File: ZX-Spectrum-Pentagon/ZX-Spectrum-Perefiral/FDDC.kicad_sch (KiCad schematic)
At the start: 39 parts

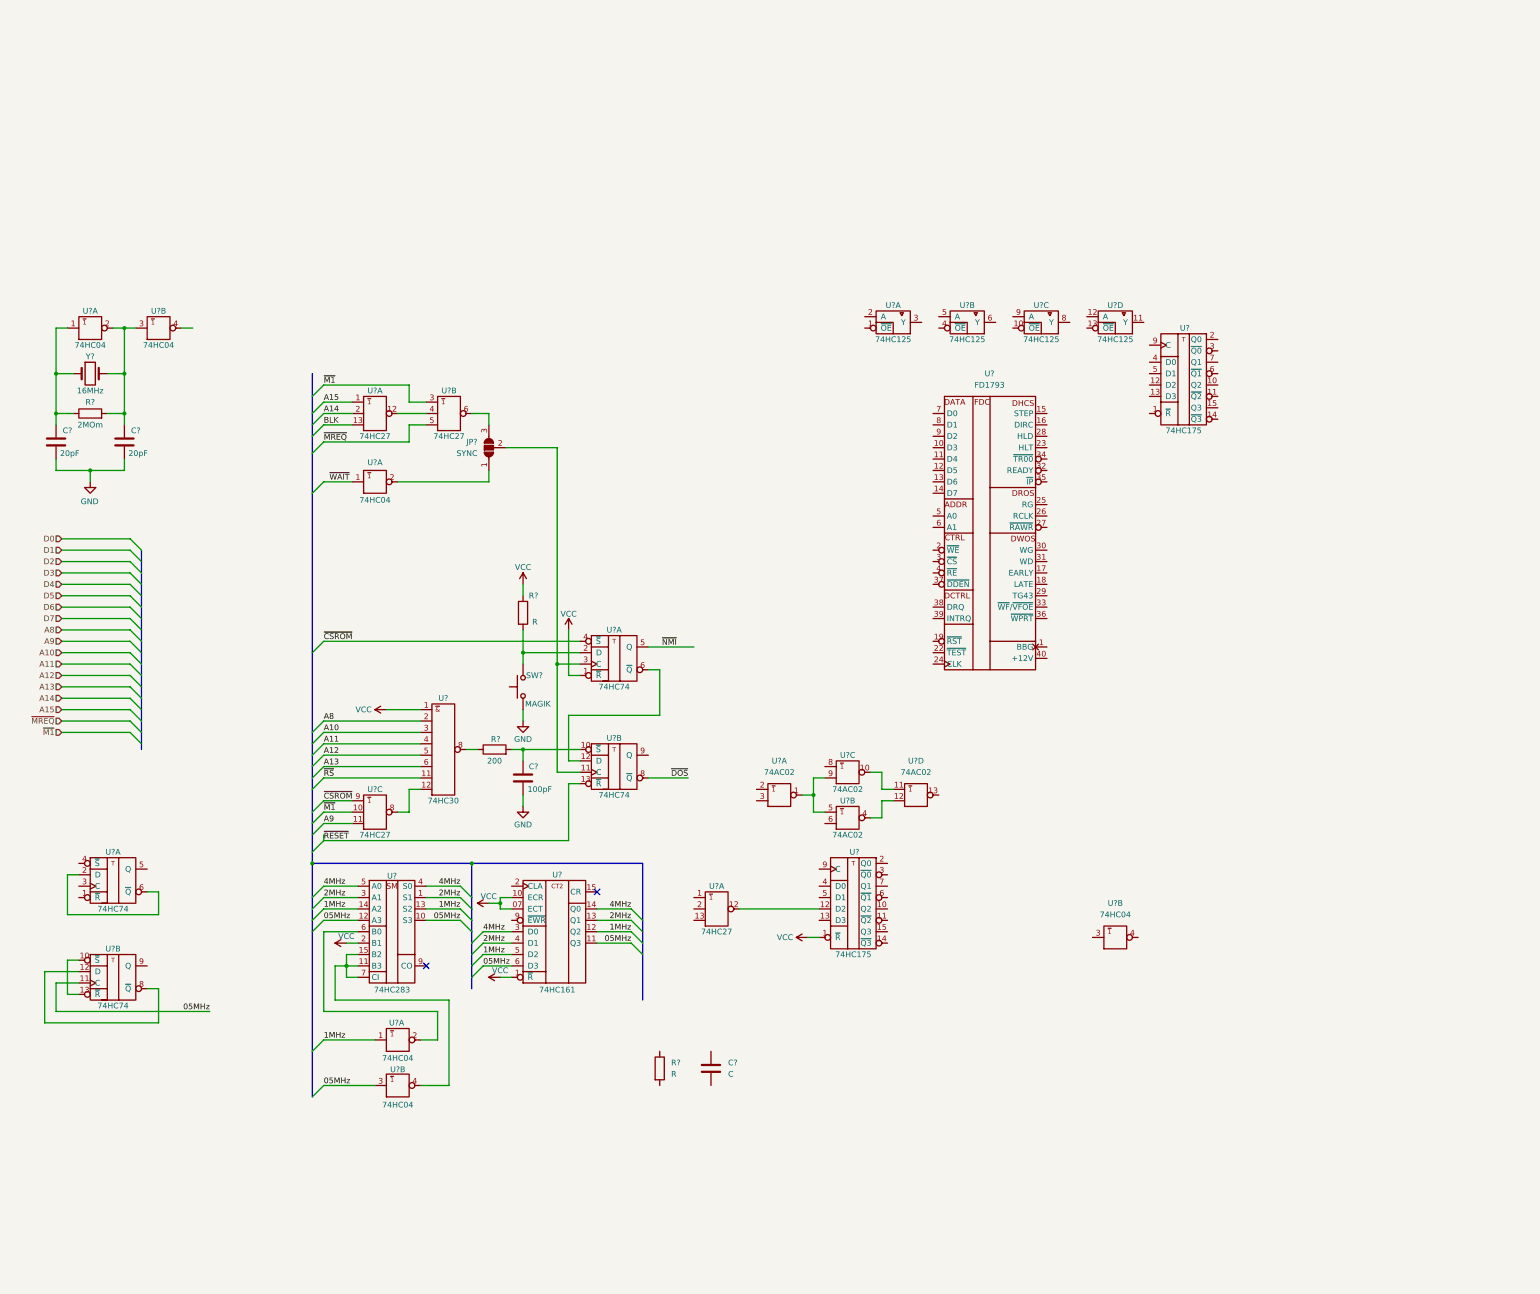
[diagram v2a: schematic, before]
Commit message: CPU.kicad_sch non functional changes update fdd controller
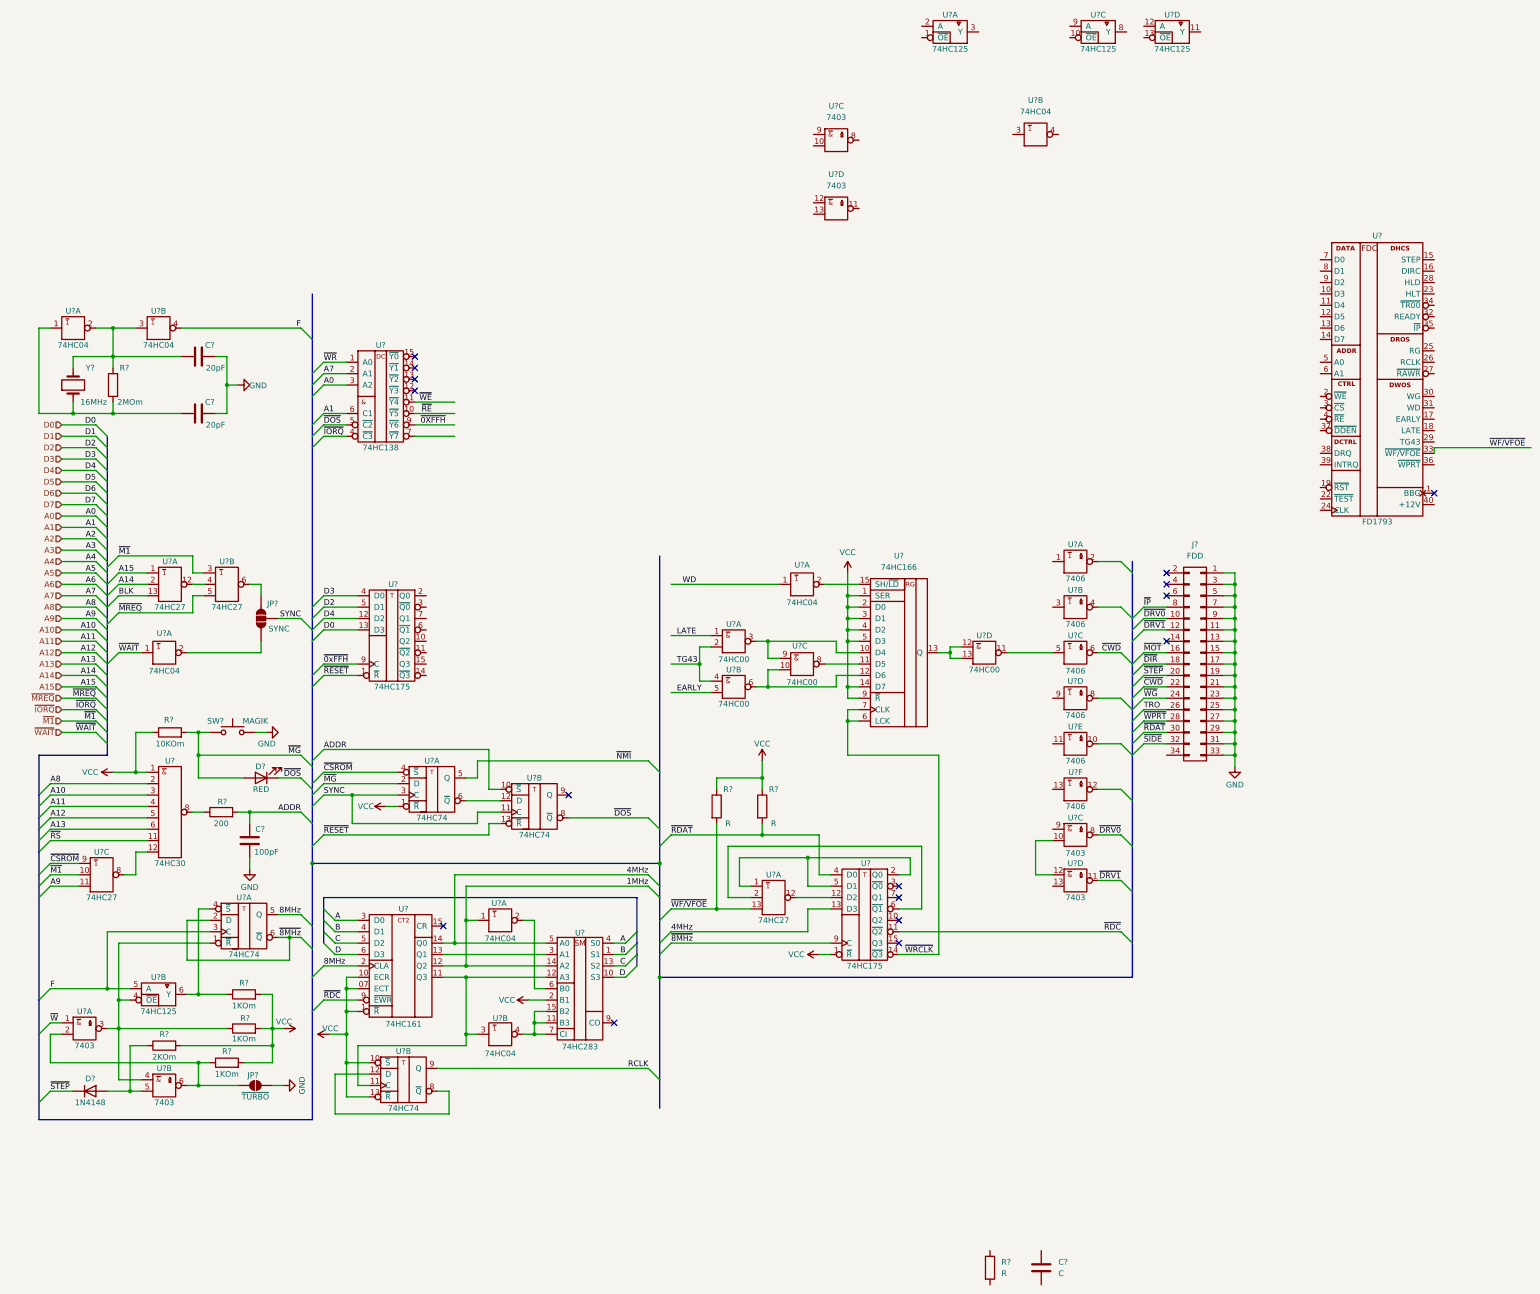
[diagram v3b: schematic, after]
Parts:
- removed R?: R, Resistor_SMD:R_0805_2012Metric, symbol Device:R
- removed SW?: MAGIK, Button_Switch_THT:SW_Tactile_SPST_Angled_PTS645Vx31-2LFS, symbol Switch:SW_Push
- removed U? (x4): 74AC02, symbol 74IEC:74AC02
- added D?: 1N4148, Diode_SMD:D_MELF, symbol Device:D
- added D?: RED, LED_SMD:LED_0805_2012Metric, symbol Device:LED
- added J?: FDD, symbol zx_custom_symbol:Conn_02x17_Odd_Even
- added JP?: ~{TURBO}, symbol Jumper:SolderJumper_2_Open
- added R? (x3): 1KOm, Resistor_SMD:R_0805_2012Metric, symbol Device:R
- added R? (x2): R, Resistor_SMD:R_0805_2012Metric, symbol Device:R
- added R?: 2KOm, Resistor_SMD:R_0805_2012Metric, symbol Device:R
- added R?: 10KOm, Resistor_SMD:R_0805_2012Metric, symbol Device:R
- added SW?: MAGIK, Button_Switch_THT:SW_Tactile_SPST_Angled_PTS645Vx31-2LFS, symbol Switch:SW_Push
- added U?: 74HC166, symbol 74IEC:74HC166
- added U? (x4): 74HC00, symbol 74IEC:74HC00
- added U? (x6): 7406, symbol 74IEC:7406
- added U? (x6): 7403, symbol 74IEC:7403
- added U?: 74HC138, symbol 74IEC:74HC138
- added U?: 74HC04, symbol 74IEC:74HC04
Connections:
- net 1MHz: no longer U?.13 (S2), U?.5 (D2)
- net 4MHz: now also U?.13 (D3); no longer U?.3 (D0), U?.4 (S0)
- net D0: now also U?.13 (D3)
- net D2: now also U?.5 (D1)
- net D3: now also U?.4 (D0)
- net D4: now also U?.12 (D2)
- net GND: now also C?.1, C?.1, J?.1 (Pin_1), J?.11 (Pin_11), J?.13 (Pin_13), J?.15 (Pin_15), J?.17 (Pin_17), J?.19 (Pin_19), J?.21 (Pin_21), J?.23 (Pin_23), J?.25 (Pin_25), J?.27 (Pin_27), J?.29 (Pin_29), J?.3 (Pin_3), J?.31 (Pin_31), J?.33 (Pin_33), J?.5 (Pin_5), J?.7 (Pin_7), J?.9 (Pin_9), JP?.1 (A), SW?.1, U?.7 (GND), U?.7 (GND), U?.7 (GND), U?.7 (GND), U?.7 (GND), U?.7 (GND), U?.7 (GND), U?.7 (GND), U?.7 (GND), U?.7 (GND), U?.7 (GND), U?.7 (GND), U?.7 (GND), U?.7 (GND), U?.7 (GND), U?.7 (GND), U?.7 (GND), U?.8 (GND), U?.8 (GND); no longer C?.2, C?.2
- net VCC: now also U?.1 (~{R}), U?.10 (~{S}), U?.13 (~{R}), R?.1, R?.1, R?.1, R?.2, R?.2, R?.2, R?.2, U?.1 (SER), U?.14 (D7), U?.14 (VCC), U?.14 (VCC), U?.14 (VCC), U?.14 (VCC), U?.14 (VCC), U?.14 (VCC), U?.14 (VCC), U?.14 (VCC), U?.14 (VCC), U?.14 (VCC), U?.14 (VCC), U?.14 (VCC), U?.14 (VCC), U?.14 (VCC), U?.14 (VCC), U?.14 (VCC), U?.14 (VCC), U?.16 (VCC), U?.2 (D0), U?.3 (D1), U?.4 (D2), U?.5 (D3), U?.9 (~{R}); no longer U?.1 (~{R})
- net ~{DOS}: now also D?.1 (K), U?.5 (~{C2})
- net ~{RESET}: now also U?.1 (~{R})
- net ~{RDC}: now reaches U?.11 (~{Q2})
- net ~{RDC}: now also U?.9 (~{EWR})
- net at U?.12 (D2): now also U?.12 (~{Y})
- net ~{WRCLK}: now reaches U?.14 (~{Q3})
- net ~{WRCLK}: now also U?.6 (LCK), U?.7 (CLK)
- net at U?.2 (Q0): now also U?.1 (A), U?.5 (D1)
- net ~{RDAT}: now reaches U?.4 (D0)
- net ~{RDAT}: now also J?.30 (Pin_30), R?.2
- net at U?.6 (~{Q1}): now also U?.2 (B)
- net ~{8MHz}: now reaches U?.9 (C)
- net ~{8MHz}: now also U?.2 (D), U?.6 (~{Q})
- net at R?.1, U?.1 (A), Y?.1: now also C?.2; no longer C?.1
- net RCLK: now reaches U?.9 (Q)
- net ~{WF/VFOE}: now reaches U?.33 (~{WF/VFOE})
- net ~{WF/VFOE}: now also U?.13 (C), R?.2
- net at R?.2, U?.2 (~{Y}), U?.3 (A)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: now also C?.2; no longer C?.1
- net F: now reaches U?.4 (~{Y})
- net F: now also U?.3 (C), U?.5 (A)
- net at U?.4 (~{OE}): now also U?.1 (~{R}), R?.1, U?.3 (~{Y}), U?.4 (A)
- net at U?.6 (Y): now also U?.4 (~{S}), R?.1
- net ~{0xFFH}: now reaches U?.9 (C)
- net SYNC: now reaches JP?.2 (C), U?.11 (C), U?.3 (C)
- net 8MHz: now reaches U?.2 (CLA)
- net 8MHz: now also U?.5 (Q)
- net ~{MG}: now reaches U?.2 (D)
- net ~{MG}: now also D?.2 (A), R?.2, SW?.2
- net ADDR: now reaches C?.1, R?.2, U?.10 (~{S})
- net 05MHz: no longer names the net of U?.11 (C), U?.11 (Q3), U?.12 (A3), U?.3 (A)
- net 05MHz: no longer U?.10 (S3), U?.6 (D3)
- net 2MHz: no longer names the net of U?.13 (Q1), U?.3 (A1)
- net 2MHz: no longer U?.1 (S1), U?.4 (D1)
- new net: U?.10 (D4), U?.3 (~{Y}), U?.9 (A)
- new net: U?.11 (D5), U?.8 (~{Y})
- new net: U?.10 (B), U?.12 (D6), U?.6 (~{Y})
- new net: U?.12 (A), U?.13 (B), U?.13 (Q)
- new net: U?.15 (SH/~{LD}), U?.2 (~{Y})
- new net: JP?.2 (B), R?.1, U?.2 (B), U?.6 (~{Y})
- new net: D?.2 (A), R?.1, U?.5 (B)
- new net: U?.11 (~{Y}), U?.5 (A)
- new net: U?.10 (B), U?.12 (A)
- new net A: U?.3 (D0), U?.4 (S0)
- new net A0: U?.3 (A2)
- new net A1: U?.6 (C1)
- new net A7: U?.2 (A1)
- new net B: U?.1 (S1), U?.4 (D1)
- new net C: U?.13 (S2), U?.5 (D2)
- new net D: U?.10 (S3), U?.6 (D3)
- new net EARLY: U?.5 (B)
- new net LATE: U?.1 (A)
- new net TG43: U?.2 (B), U?.4 (A)
- new net TRO: J?.26 (Pin_26)
- new net VСС: U?.16 (VСС)
- new net WD: U?.1 (A)
- new net ~{0XFFH}: U?.9 (~{Y6})
- new net ~{CWD}: J?.22 (Pin_22), U?.6 (~{Y})
- new net ~{DIR}: J?.18 (Pin_18)
- new net ~{DRV0}: J?.10 (Pin_10), U?.8 (~{Y})
- new net ~{DRV1}: J?.12 (Pin_12), U?.11 (~{Y})
- new net ~{IORQ}: U?.4 (~{C3})
- new net ~{IP}: J?.8 (Pin_8)
- new net ~{MOT}: J?.16 (Pin_16)
- new net ~{RE}: U?.10 (~{Y5})
- new net ~{SIDE}: J?.32 (Pin_32)
- new net ~{STEP}: D?.1 (K), J?.20 (Pin_20)
- new net ~{WE}: U?.11 (~{Y4})
- new net ~{WG}: J?.24 (Pin_24)
- new net ~{WPRT}: J?.28 (Pin_28)
- new net ~{WR}: U?.1 (A0)
- new net ~{W}: U?.1 (A)
- no-connect marks 2 -> 16
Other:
- moved on the sheet: C?, R?, U?, U?A, U?B, U?C, U?D, Y?

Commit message: update schematic FDC
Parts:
- removed R?: R, Resistor_SMD:R_0805_2012Metric, symbol Device:R
- removed U? (x2): 74HC125, symbol 74IEC:74HC125
- added D? (x2): D, symbol Device:D
- added R? (x2): R, Resistor_SMD:R_0805_2012Metric, symbol Device:R
- added R?: 1KOm, Resistor_SMD:R_0805_2012Metric, symbol Device:R
- added R?: 1kOm, Resistor_SMD:R_0805_2012Metric, symbol Device:R
- added R? (x2): 10kOm, Resistor_SMD:R_0805_2012Metric, symbol Device:R
- added U? (x2): 74HC367, symbol 74IEC:74HC367
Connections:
- net ~{0xFFH} is gone; now on net ~{WRSYS}: U?.9 (C)
- net ~{DIR} is gone; now on net ~{DIRC}: J?.18 (Pin_18)
- net ~{RDC} is gone; now on net ~{RAWR}: U?.11 (~{Q2}), U?.9 (~{EWR})
- net 1MHz: now also U?.24 (CLK)
- net A5: now also U?.5 (A0)
- net A6: now also U?.6 (A1)
- net A7: now also U?.3 (~{CS})
- net D0: now also U?.4 (D0), U?.7 (D0); no longer U?.13 (D3)
- net D1: now also U?.8 (D1)
- net D2: now also U?.9 (D2)
- net D3: now also U?.10 (D3), U?.12 (D2); no longer U?.4 (D0)
- net D4: now also U?.11 (D4), U?.13 (D3); no longer U?.12 (D2)
- net D5: now also U?.12 (D5)
- net D6: now also U?.13 (D6), U?.13 (B)
- net D7: now also U?.14 (D7), U?.11 (A)
- net EARLY: now also U?.17 (EARLY)
- net GND: now also U?.37 (~{DDEN}), U?.8 (GND), U?.8 (GND)
- net LATE: now also U?.18 (LATE)
- net RCLK: now also U?.26 (RCLK)
- net VCC: now also U?.22 (~{TEST}), D?.2 (A), R?.2, R?.2, R?.2, R?.2, R?.2, R?.2, U?.16 (VCC), U?.16 (VCC)
- net WD: now also U?.29 (TG43), U?.31 (WD)
- net ~{DRV0}: now also U?.3 (~{Q0}), U?.9 (A); no longer J?.10 (Pin_10), U?.8 (~{Y})
- net ~{IP}: now also U?.35 (~{IP}), R?.1, U?.9 (D); no longer J?.8 (Pin_8)
- net ~{MOT}: now also U?.8 (~{Y})
- net ~{RE}: now also U?.4 (~{RE})
- net ~{SIDE}: now also U?.12 (~{Y})
- net ~{STEP}: now also U?.2 (~{Y})
- net ~{WE}: now also U?.2 (~{WE})
- net ~{WG}: now also U?.10 (~{Y})
- net ~{WPRT}: now also U?.36 (~{WPRT}), R?.1, U?.3 (A); no longer J?.28 (Pin_28)
- net SIDE: now reaches U?.13 (A)
- net SIDE: now also U?.14 (~{Q3})
- net STEP: now reaches U?.15 (STEP)
- net STEP: now also U?.1 (A)
- net DIRC: now reaches U?.16 (DIRC)
- net DIRC: now also U?.3 (A)
- net ~{CRST}: now reaches U?.19 (~{RST})
- net ~{CRST}: now also U?.7 (Q1)
- net HLT: now reaches U?.23 (HLT)
- net HLT: now also U?.10 (Q2)
- net ~{RAWR}: now reaches U?.27 (~{RAWR})
- net MOT: now reaches U?.28 (HLD)
- net MOT: now also U?.10 (B), U?.12 (A), U?.32 (READY), U?.9 (A)
- net WG: now reaches U?.30 (WG)
- net WG: now also U?.11 (A)
- net ~{TR00}: now reaches U?.34 (~{TR00})
- net DRQ: now reaches U?.38 (DRQ)
- net DRQ: now also R?.1, U?.14 (B)
- net INTRQ: now reaches U?.39 (INTRQ)
- net INTRQ: now also R?.1, U?.12 (A)
- net FDCPW: now reaches U?.40 (+12V)
- net FDCPW: now also D?.1 (K), D?.1 (K)
- net DRV0: now reaches U?.2 (Q0)
- net DRV0: now also U?.13 (B)
- net ~{DIRC}: now reaches U?.4 (~{Y})
- net ~{RDSYS}: now reaches U?.7 (~{Y7})
- net ~{RDSYS}: now also U?.15 (~{OE})
- net TRO renamed ~{TR0_}
- net ~{TR0_}: now also U?.6 (C)
- net ~{0XFFH} renamed ~{WRSYS}
- net ~{CWD} renamed ~{WRDAT}
- net ~{DRV1} renamed ~{DS1}
- net ~{RDAT} renamed ~{RDDAT_}
- net ~{RDDAT_}: now also U?.4 (B); no longer U?.4 (D0)
- net ~{WF/VFOE} renamed ~{WFDE}
- net ~{WRCLK}: no longer names the net of U?.14 (~{Q3}), U?.6 (LCK), U?.7 (CLK)
- new net +12: D?.2 (A)
- new net ~{DS0}: J?.10 (Pin_10), U?.8 (~{Y})
- new net ~{IP_}: J?.8 (Pin_8), U?.10 (D)
- new net ~{RDDAT}: R?.1, U?.4 (D0), U?.5 (B)
- new net ~{TR0}: R?.1, U?.7 (C)
- new net ~{WPRT_}: J?.28 (Pin_28), U?.2 (A)
- no-connect marks 16 -> 20
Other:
- moved on the sheet: C?, J?, R?, U?, U?A, U?B, U?C, U?D, U?E, U?F, Y?
